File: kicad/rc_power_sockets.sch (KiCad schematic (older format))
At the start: 20 parts, among them IC1 ATTINY85-S, J1 Motion Sensor, J2 Radio 433MHZ, P1 ICSP, Q1 Q_NMOS_GSD, Q2 Q_PMOS_GSD, SW1 Power Switch, U1 MCP1700T-3302E/TT

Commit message: Layout
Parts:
- removed SW1: Power Switch, Buttons_Switches_ThroughHole:SW_Micro_SPST, symbol SWITCH_INV
- added SW1: SPST, Pin_Headers:Pin_Header_Straight_1x02, symbol SPST
- RV1: footprint Potentiometers:Potentiometer_WirePads_largePads -> Potentiometers:Potentiometer_WirePads_Small
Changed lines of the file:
@@
 	4900 5050 4300 5050
 Wire Wire Line
-	4900 5550 4300 5550
+	4300 5550 4900 5550
 Wire Wire Line
 	9100 2450 8750 2450
@@
 	9800 2350 10000 2350
 Wire Wire Line
-	6800 1050 6800 1450
+	6800 1050 6800 1550
 Wire Wire Line
 	4900 5450 4300 5450
@@
 $EndComp
 $Comp
-L SWITCH_INV SW1
-U 1 1 56D9E668
-P 6300 1550
-F 0 "SW1" H 6100 1700 50  0000 C CNN
-F 1 "Power Switch" H 6150 1400 50  0000 C CNN
-F 2 "Buttons_Switches_ThroughHole:SW_Micro_SPST" H 6300 1550 50  0001 C CNN
-F 3 "" H 6300 1550 50  0000 C CNN
-	1    6300 1550
-	1    0    0    -1
-$EndComp
-$Comp
-L GND #PWR08
-U 1 1 56D9E7B6
-P 6800 1650
-F 0 "#PWR08" H 6800 1400 50  0001 C CNN
-F 1 "GND" H 6800 1500 50  0000 C CNN
-F 2 "" H 6800 1650 50  0000 C CNN
-F 3 "" H 6800 1650 50  0000 C CNN
-	1    6800 1650
-	1    0    0    -1
-$EndComp
-$Comp
 L POT RV1
 U 1 1 56E809B9
@@
 F 0 "RV1" H 9650 5220 50  0000 C CNN
 F 1 "POT" H 9650 5300 50  0000 C CNN
-F 2 "Potentiometers:Potentiometer_WirePads_largePads" H 9650 5300 50  0001 C CNN
+F 2 "Potentiometers:Potentiometer_WirePads_Small" H 9650 5300 50  0001 C CNN
 F 3 "" H 9650 5300 50  0000 C CNN
 	1    9650 5300
@@
 $EndComp
 $Comp
-L GND #PWR09
+L GND #PWR08
 U 1 1 56E80AFC
 P 9650 5750
-F 0 "#PWR09" H 9650 5500 50  0001 C CNN
+F 0 "#PWR08" H 9650 5500 50  0001 C CNN
 F 1 "GND" H 9650 5600 50  0000 C CNN
 F 2 "" H 9650 5750 50  0000 C CNN
@@
 $EndComp
 $Comp
-L VCC #PWR010
+L VCC #PWR09
 U 1 1 56E80BFE
 P 6800 1050
-F 0 "#PWR010" H 6800 900 50  0001 C CNN
+F 0 "#PWR09" H 6800 900 50  0001 C CNN
 F 1 "VCC" H 6800 1200 50  0000 C CNN
 F 2 "" H 6800 1050 50  0000 C CNN
@@
 	1    0    0    -1
 $EndComp
+$Comp
+L SPST SW1
+U 1 1 56EAAC50
+P 6300 1550
+F 0 "SW1" H 6300 1650 50  0000 C CNN
+F 1 "SPST" H 6300 1450 50  0000 C CNN
+F 2 "Pin_Headers:Pin_Header_Straight_1x02" H 6300 1550 50  0001 C CNN
+F 3 "" H 6300 1550 50  0000 C CNN
+	1    6300 1550
+	1    0    0    -1
+$EndComp

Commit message: Layout change
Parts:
- removed JP1: Jumper_NO_Small, Pin_Headers:Pin_Header_Straight_1x02, symbol Jumper_NO_Small
- removed R5: 100K, Resistors_SMD:R_0805_HandSoldering, symbol R
- IC1: value ATTINY85-S -> ATTINY85
- J1: value Motion Sensor -> Motion
- J2: value Radio 433MHZ -> 433MHZ
- Q1: value Q_NMOS_GSD -> NMOS
- Q2: value Q_PMOS_GSD -> PMOS
- RV1: symbol POT -> POT-RESCUE-rc_power_sockets
- U1: value MCP1700T-3302E/TT -> MCP1700T
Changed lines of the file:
@@
 EESchema Schematic File Version 2
+LIBS:rc_power_sockets-rescue
 LIBS:power
 LIBS:device
@@
 	1    0    0    -1
 $EndComp
-$Comp
-L Jumper_NO_Small JP1
-U 1 1 56D7129A
-P 9800 2150
-F 0 "JP1" H 9800 2230 50  0000 C CNN
-F 1 "Jumper_NO_Small" H 9810 2090 50  0001 C CNN
-F 2 "Pin_Headers:Pin_Header_Straight_1x02" H 9800 2150 50  0001 C CNN
-F 3 "" H 9800 2150 50  0000 C CNN
-	1    9800 2150
-	0    1    1    0
-$EndComp
 Text Label 4300 5450 0    60   ~ 0
 RADIO_DATA
@@
 P 3000 2050
 F 0 "J1" H 3000 2250 50  0000 C CNN
-F 1 "Motion Sensor" H 3000 1750 50  0000 C CNB
+F 1 "Motion" H 3000 1750 50  0000 C CNB
 F 2 "Socket_Strips:Socket_Strip_Straight_1x03" H 3050 2050 50  0001 C CNN
 F 3 "" H 3050 2050 50  0000 C CNN
@@
 P 9750 3450
 F 0 "J2" H 9750 3250 50  0000 C CNN
-F 1 "Radio 433MHZ" H 9750 3750 50  0000 C CNB
+F 1 "433MHZ" H 9750 3750 50  0000 C CNB
 F 2 "Socket_Strips:Socket_Strip_Straight_1x03" H 9800 3450 50  0001 C CNN
 F 3 "" H 9800 3450 50  0000 C CNN
@@
 	3700 5250 4900 5250
 Wire Wire Line
-	9800 1950 9800 2050
+	9800 1950 9800 2250
 Connection ~ 6550 1950
 Wire Wire Line
@@
 P 6250 5300
 F 0 "IC1" H 5100 5700 50  0000 C CNN
-F 1 "ATTINY85-S" H 7250 4900 50  0000 C CNN
+F 1 "ATTINY85" H 7250 4900 50  0000 C CNN
 F 2 "SMD_Packages:SOIC-8-N" H 7200 5300 50  0000 C CIN
 F 3 "" H 6250 5300 50  0000 C CNN
@@
 $EndComp
 $Comp
-L POT RV1
+L POT-RESCUE-rc_power_sockets RV1
 U 1 1 56E809B9
 P 9650 5300
@@
 L GND #PWR08
 U 1 1 56E80AFC
-P 9650 5750
-F 0 "#PWR08" H 9650 5500 50  0001 C CNN
-F 1 "GND" H 9650 5600 50  0000 C CNN
-F 2 "" H 9650 5750 50  0000 C CNN
-F 3 "" H 9650 5750 50  0000 C CNN
-	1    9650 5750
+P 9650 5450
+F 0 "#PWR08" H 9650 5200 50  0001 C CNN
+F 1 "GND" H 9650 5300 50  0000 C CNN
+F 2 "" H 9650 5450 50  0000 C CNN
+F 3 "" H 9650 5450 50  0000 C CNN
+	1    9650 5450
 	1    0    0    -1
 $EndComp
@@
 Wire Wire Line
 	9650 5050 9650 5150
-$Comp
-L R R5
-U 1 1 56E80FD3
-P 9650 5600
-F 0 "R5" V 9730 5600 50  0000 C CNN
-F 1 "100K" V 9650 5600 50  0000 C CNN
-F 2 "Resistors_SMD:R_0805_HandSoldering" V 9580 5600 50  0001 C CNN
-F 3 "" H 9650 5600 50  0000 C CNN
-	1    9650 5600
-	1    0    0    -1
-$EndComp
 Text Label 4300 5350 0    60   ~ 0
 ADC3
@@
 P 6450 2450
 F 0 "Q2" H 6750 2500 50  0000 R CNN
-F 1 "Q_PMOS_GSD" H 7100 2400 50  0000 R CNN
+F 1 "PMOS" H 6850 2400 50  0000 R CNN
 F 2 "TO_SOT_Packages_SMD:SOT-23_Handsoldering" H 6650 2550 50  0001 C CNN
 F 3 "" H 6450 2450 50  0000 C CNN
@@
 P 5450 3150
 F 0 "Q1" H 5750 3200 50  0000 R CNN
-F 1 "Q_NMOS_GSD" H 6100 3100 50  0000 R CNN
+F 1 "NMOS" H 5850 3100 50  0000 R CNN
 F 2 "TO_SOT_Packages_SMD:SOT-23_Handsoldering" H 5650 3250 50  0001 C CNN
 F 3 "" H 5450 3150 50  0000 C CNN
@@
 P 7350 3900
 F 0 "U1" H 7500 3600 50  0000 C CNN
-F 1 "MCP1700T-3302E/TT" H 7350 4100 50  0000 C CNN
+F 1 "MCP1700T" H 7350 4100 50  0000 C CNN
 F 2 "TO_SOT_Packages_SMD:SOT-23_Handsoldering" H 7350 4000 50  0000 C CIN
 F 3 "" H 7350 3900 50  0000 C CNN

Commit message: Traces
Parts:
- removed P1: ICSP, Pin_Headers:Pin_Header_Straight_2x03, symbol DIL6
- added J3: 433MHZ, Socket_Strips:Socket_Strip_Straight_1x03, symbol SIL3
- added P1: ICSP, Pin_Headers:Pin_Header_Straight_2x03, symbol CONN_02X03
- added P2: CONN_GND, Pin_Headers:Pin_Header_Straight_1x01, symbol CONN_01X01
- J1: value Motion -> PIR
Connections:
- net GND: now also J3.1, P1.6 (P6), P2.1 (P1)
- net MISO: now also P1.1 (P1)
- net MOSI: now also P1.4 (P4)
- net RADIO_DATA: now also J2.3, J3.3; no longer J2.2
- net RESET: now also RV1.3, P1.5 (P5)
- net SCK: now also P1.3 (P3)
- net NBASE: now reaches Q1.1 (G), R1.1, R3.1
- net NBASE_ON: now reaches D1.1 (K), D2.1 (K), R1.2
- net POWER: now reaches J1.3, Q2.3 (D), R2.1, SW1.1
- net POWER: now also P1.2 (P2)
- net PBASE: now reaches Q1.3 (D), Q2.1 (G), R2.2
- net 3.3v: now reaches C2.1, C3.1, IC1.8 (VCC), R4.2, U1.2 (VOUT)
- net 3.3v: no longer RV1.3
- net SWITCH_POWER: now reaches C1.1, Q2.2 (S), U1.3 (VIN)
- net SWITCH_POWER: now also J2.2, J3.2; no longer J2.3
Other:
- moved on the sheet: RV1
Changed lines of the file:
@@
 Text Label 4300 5550 0    60   ~ 0
 RESET
-Text Label 10000 2350 0    60   ~ 0
+Text Label 8600 2300 0    60   ~ 0
 MOSI
-Text Label 8750 2250 0    60   ~ 0
+Text Label 7650 2200 0    60   ~ 0
 MISO
-Text Label 8750 2450 0    60   ~ 0
+Text Label 7650 2400 0    60   ~ 0
 RESET
-$Comp
-L DIL6 P1
-U 1 1 56D70BCB
-P 9450 2350
-F 0 "P1" H 9450 2550 50  0000 C CNN
-F 1 "ICSP" H 9450 2100 50  0000 C CNB
-F 2 "Pin_Headers:Pin_Header_Straight_2x03" H 9450 2350 50  0001 C CNN
-F 3 "" H 9450 2350 50  0000 C CNN
-	1    9450 2350
-	1    0    0    -1
-$EndComp
-Text Label 8750 2350 0    60   ~ 0
+Text Label 7650 2300 0    60   ~ 0
 SCK
 $Comp
 L GND #PWR04
 U 1 1 56D7102B
-P 9800 2450
-F 0 "#PWR04" H 9800 2200 50  0001 C CNN
-F 1 "GND" H 9800 2300 50  0000 C CNN
-F 2 "" H 9800 2450 50  0000 C CNN
-F 3 "" H 9800 2450 50  0000 C CNN
-	1    9800 2450
+P 8450 2400
+F 0 "#PWR04" H 8450 2150 50  0001 C CNN
+F 1 "GND" H 8450 2250 50  0000 C CNN
+F 2 "" H 8450 2400 50  0000 C CNN
+F 3 "" H 8450 2400 50  0000 C CNN
+	1    8450 2400
 	1    0    0    -1
 $EndComp
@@
 P 3000 2050
 F 0 "J1" H 3000 2250 50  0000 C CNN
-F 1 "Motion" H 3000 1750 50  0000 C CNB
+F 1 "PIR" H 3000 1750 50  0000 C CNB
 F 2 "Socket_Strips:Socket_Strip_Straight_1x03" H 3050 2050 50  0001 C CNN
 F 3 "" H 3050 2050 50  0000 C CNN
@@
 	1    0    0    1
 $EndComp
-Text Label 8850 3450 0    60   ~ 0
+Text Label 8850 3350 0    60   ~ 0
 RADIO_DATA
 $Comp
@@
 	1    0    0    -1
 $EndComp
-Connection ~ 5550 1950
-Wire Wire Line
-	5550 2450 6250 2450
-Wire Wire Line
-	5550 2400 5550 2950
-Wire Wire Line
-	6550 1950 6550 2250
-Connection ~ 5550 2450
-Wire Wire Line
-	6550 3850 6900 3850
-Connection ~ 6700 3850
-Wire Wire Line
-	7800 3850 8600 3850
-Wire Wire Line
-	7350 4200 7350 4400
-Wire Wire Line
-	6700 4150 6700 4300
-Wire Wire Line
-	6700 4300 8000 4300
-Connection ~ 7350 4300
-Wire Wire Line
-	8000 4300 8000 4150
-Wire Wire Line
-	8600 3850 8600 5950
-Wire Wire Line
-	7600 5050 9650 5050
-Connection ~ 8000 3850
-Wire Wire Line
-	4150 3050 4150 3300
-Connection ~ 4150 3150
-Wire Wire Line
-	4150 2050 4150 2750
-Wire Wire Line
-	4150 5150 4900 5150
-Wire Wire Line
-	4900 5050 4300 5050
-Wire Wire Line
-	4300 5550 4900 5550
-Wire Wire Line
-	9100 2450 8750 2450
-Wire Wire Line
-	9100 2350 8750 2350
-Wire Wire Line
-	9100 2250 8750 2250
-Wire Wire Line
-	9800 2350 10000 2350
-Wire Wire Line
-	6800 1050 6800 1550
-Wire Wire Line
-	4900 5450 4300 5450
-Wire Wire Line
-	3350 1950 9800 1950
-Wire Wire Line
-	4150 3600 4150 5150
-Wire Wire Line
-	5550 1550 5800 1550
-Wire Wire Line
-	4650 3150 4150 3150
-Wire Wire Line
-	4950 3150 5250 3150
-Wire Wire Line
-	6550 2650 6550 3850
-Wire Wire Line
-	9400 3450 8850 3450
-Wire Wire Line
-	3350 2050 4150 2050
-Wire Wire Line
-	3700 2050 3700 5250
-Connection ~ 3700 2050
-Wire Wire Line
-	3700 5250 4900 5250
-Wire Wire Line
-	9800 1950 9800 2250
-Connection ~ 6550 1950
-Wire Wire Line
-	5550 1550 5550 2100
-Connection ~ 6550 3350
-Wire Wire Line
-	5550 3350 5550 3800
 $Comp
 L R R3
@@
 	1    0    0    -1
 $EndComp
-Wire Wire Line
-	5150 3650 5550 3650
-Connection ~ 5550 3650
-Wire Wire Line
-	5150 3350 5150 3150
-Connection ~ 5150 3150
 $Comp
 L R R4
@@
 	1    0    0    -1
 $EndComp
-Wire Wire Line
-	4750 5650 4750 5550
-Connection ~ 4750 5550
-Wire Wire Line
-	8600 5950 4750 5950
-Connection ~ 8600 5050
-Wire Wire Line
-	9400 3350 6550 3350
 $Comp
 L C C3
@@
 	1    0    0    -1
 $EndComp
-Wire Wire Line
-	8250 5200 8250 5050
-Connection ~ 8250 5050
 $Comp
 L GND #PWR07
@@
 L POT-RESCUE-rc_power_sockets RV1
 U 1 1 56E809B9
-P 9650 5300
-F 0 "RV1" H 9650 5220 50  0000 C CNN
-F 1 "POT" H 9650 5300 50  0000 C CNN
-F 2 "Potentiometers:Potentiometer_WirePads_Small" H 9650 5300 50  0001 C CNN
-F 3 "" H 9650 5300 50  0000 C CNN
-	1    9650 5300
+P 4100 6050
+F 0 "RV1" H 4100 5970 50  0000 C CNN
+F 1 "POT" H 4100 6050 50  0000 C CNN
+F 2 "Potentiometers:Potentiometer_WirePads_Small" H 4100 6050 50  0001 C CNN
+F 3 "" H 4100 6050 50  0000 C CNN
+	1    4100 6050
 	0    -1   -1   0
 $EndComp
@@
 L GND #PWR08
 U 1 1 56E80AFC
-P 9650 5450
-F 0 "#PWR08" H 9650 5200 50  0001 C CNN
-F 1 "GND" H 9650 5300 50  0000 C CNN
-F 2 "" H 9650 5450 50  0000 C CNN
-F 3 "" H 9650 5450 50  0000 C CNN
-	1    9650 5450
+P 4100 6200
+F 0 "#PWR08" H 4100 5950 50  0001 C CNN
+F 1 "GND" H 4100 6050 50  0000 C CNN
+F 2 "" H 4100 6200 50  0000 C CNN
+F 3 "" H 4100 6200 50  0000 C CNN
+	1    4100 6200
 	1    0    0    -1
 $EndComp
@@
 	1    0    0    -1
 $EndComp
-Wire Wire Line
-	9650 5050 9650 5150
 Text Label 4300 5350 0    60   ~ 0
 ADC3
-Text Label 9200 5300 0    60   ~ 0
+Text Label 3650 6050 0    60   ~ 0
 ADC3
-Wire Wire Line
-	9500 5300 9200 5300
-Wire Wire Line
-	4900 5350 4300 5350
 $Comp
 L Q_PMOS_GSD Q2
@@
 	1    0    0    -1
 $EndComp
+$Comp
+L CONN_02X03 P1
+U 1 1 56EEE1EA
+P 8200 2300
+F 0 "P1" H 8200 2500 50  0000 C CNN
+F 1 "ICSP" H 8200 2100 50  0000 C CNN
+F 2 "Pin_Headers:Pin_Header_Straight_2x03" H 8200 1100 50  0001 C CNN
+F 3 "" H 8200 1100 50  0000 C CNN
+	1    8200 2300
+	1    0    0    -1
+$EndComp
+Text Label 4200 3150 0    60   ~ 0
+NBASE_ON
+Text Label 5850 2450 0    60   ~ 0
+PBASE
+Text Label 8600 4400 0    60   ~ 0
+3.3v
+Text Label 6550 3050 0    60   ~ 0
+SWITCH_POWER
+Text Label 4600 1950 0    60   ~ 0
+POWER
+Text Label 5000 3150 0    60   ~ 0
+NBASE
+$Comp
+L CONN_01X01 P2
+U 1 1 56EEF3F5
+P 7200 1000
+F 0 "P2" V 7150 900 50  0000 C CNN
+F 1 "CONN_GND" V 7300 1000 50  0000 C CNN
+F 2 "Pin_Headers:Pin_Header_Straight_1x01" H 7200 1000 50  0001 C CNN
+F 3 "" H 7200 1000 50  0000 C CNN
+	1    7200 1000
+	0    -1   -1   0
+$EndComp
+$Comp
+L GND #PWR010
+U 1 1 56EEF4F7
+P 7200 1200
+F 0 "#PWR010" H 7200 950 50  0001 C CNN
+F 1 "GND" H 7200 1050 50  0000 C CNN
+F 2 "" H 7200 1200 50  0000 C CNN
+F 3 "" H 7200 1200 50  0000 C CNN
+	1    7200 1200
+	1    0    0    -1
+$EndComp
+$Comp
+L SIL3 J3
+U 1 1 56EEFA66
+P 9750 2800
+F 0 "J3" H 9750 2600 50  0000 C CNN
+F 1 "433MHZ" H 9750 3100 50  0000 C CNB
+F 2 "Socket_Strips:Socket_Strip_Straight_1x03" H 9800 2800 50  0001 C CNN
+F 3 "" H 9800 2800 50  0000 C CNN
+	1    9750 2800
+	1    0    0    1
+$EndComp
+Text Label 8850 2700 0    60   ~ 0
+RADIO_DATA
+$Comp
+L GND #PWR011
+U 1 1 56EEFB0C
+P 9400 2900
+F 0 "#PWR011" H 9400 2650 50  0001 C CNN
+F 1 "GND" H 9400 2750 50  0000 C CNN
+F 2 "" H 9400 2900 50  0000 C CNN
+F 3 "" H 9400 2900 50  0000 C CNN
+	1    9400 2900
+	1    0    0    -1
+$EndComp
+Connection ~ 5550 1950
+Wire Wire Line
+	5550 2450 6250 2450
+Wire Wire Line
+	5550 2400 5550 2950
+Wire Wire Line
+	6550 1950 6550 2250
+Connection ~ 5550 2450
+Wire Wire Line
+	6550 3850 6900 3850
+Connection ~ 6700 3850
+Wire Wire Line
+	7800 3850 8600 3850
+Wire Wire Line
+	7350 4200 7350 4400
+Wire Wire Line
+	6700 4150 6700 4300
+Wire Wire Line
+	6700 4300 8000 4300
+Connection ~ 7350 4300
+Wire Wire Line
+	8000 4300 8000 4150
+Wire Wire Line
+	8600 3850 8600 5950
+Connection ~ 8000 3850
+Wire Wire Line
+	4150 3050 4150 3300
+Connection ~ 4150 3150
+Wire Wire Line
+	4150 2050 4150 2750
+Wire Wire Line
+	4150 5150 4900 5150
+Wire Wire Line
+	4900 5050 4300 5050
+Wire Wire Line
+	4100 5550 4900 5550
+Wire Wire Line
+	6800 1050 6800 1550
+Wire Wire Line
+	4900 5450 4300 5450
+Wire Wire Line
+	3350 1950 8650 1950
+Wire Wire Line
+	4150 3600 4150 5150
+Wire Wire Line
+	5550 1550 5800 1550
+Wire Wire Line
+	4650 3150 4150 3150
+Wire Wire Line
+	4950 3150 5250 3150
+Wire Wire Line
+	6550 2650 6550 3850
+Wire Wire Line
+	6550 3450 9400 3450
+Wire Wire Line
+	3350 2050 4150 2050
+Wire Wire Line
+	3700 5250 4900 5250
+Connection ~ 6550 1950
+Wire Wire Line
+	5550 1550 5550 2100
+Wire Wire Line
+	5550 3350 5550 3800
+Wire Wire Line
+	5150 3650 5550 3650
+Connection ~ 5550 3650
+Wire Wire Line
+	5150 3350 5150 3150
+Connection ~ 5150 3150
+Wire Wire Line
+	4750 5650 4750 5550
+Connection ~ 4750 5550
+Wire Wire Line
+	8600 5950 4750 5950
+Connection ~ 8600 5050
+Wire Wire Line
+	8250 5200 8250 5050
+Connection ~ 8250 5050
+Wire Wire Line
+	3950 6050 3650 6050
+Wire Wire Line
+	4900 5350 4300 5350
+Connection ~ 6550 3450
+Wire Wire Line
+	8850 3350 9400 3350
+Wire Wire Line
+	8450 2300 8600 2300
+Wire Wire Line
+	8450 2200 8650 2200
+Wire Wire Line
+	8650 2200 8650 1950
+Wire Wire Line
+	7950 2200 7650 2200
+Wire Wire Line
+	7650 2300 7950 2300
+Wire Wire Line
+	7650 2400 7950 2400
+Wire Wire Line
+	3700 2050 3700 5250
+Connection ~ 3700 2050
+Wire Wire Line
+	9400 2700 8850 2700
+Wire Wire Line
+	9400 2800 8500 2800
+Wire Wire Line
+	8500 2800 8500 3450
+Connection ~ 8500 3450
+Wire Wire Line
+	7600 5050 8600 5050
+Wire Wire Line
+	4100 5550 4100 5900
 $EndSCHEMATC

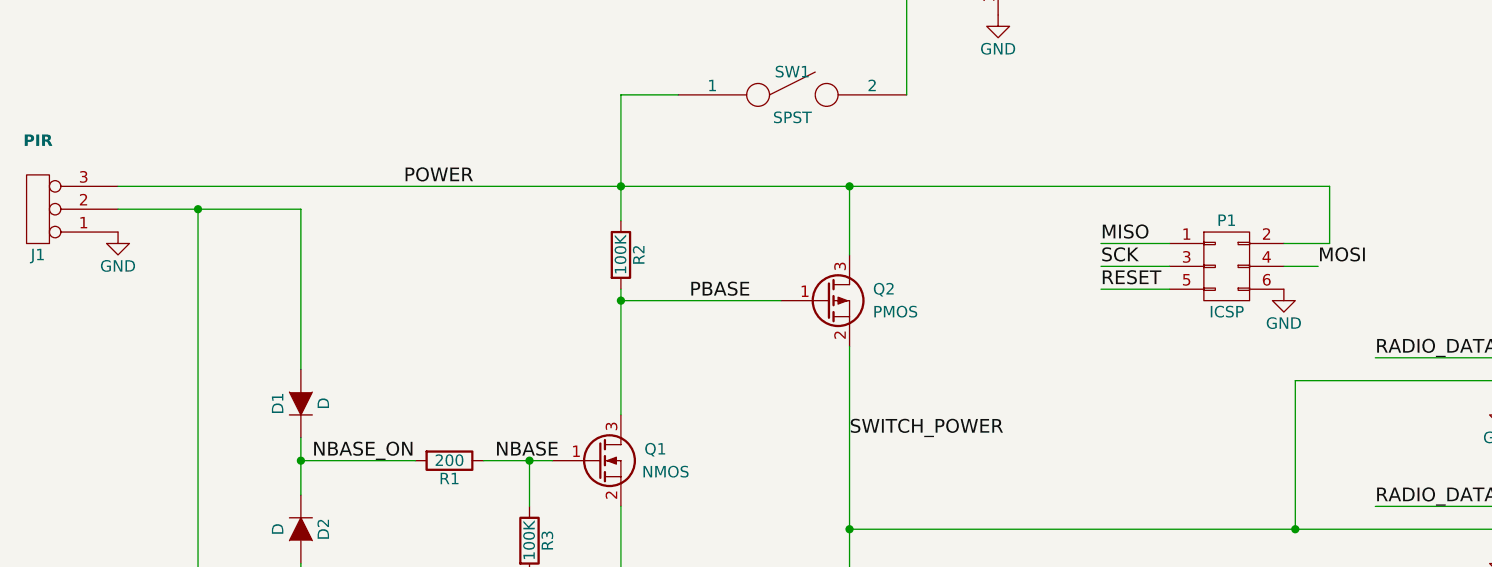
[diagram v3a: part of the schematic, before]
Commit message: Switched power plane
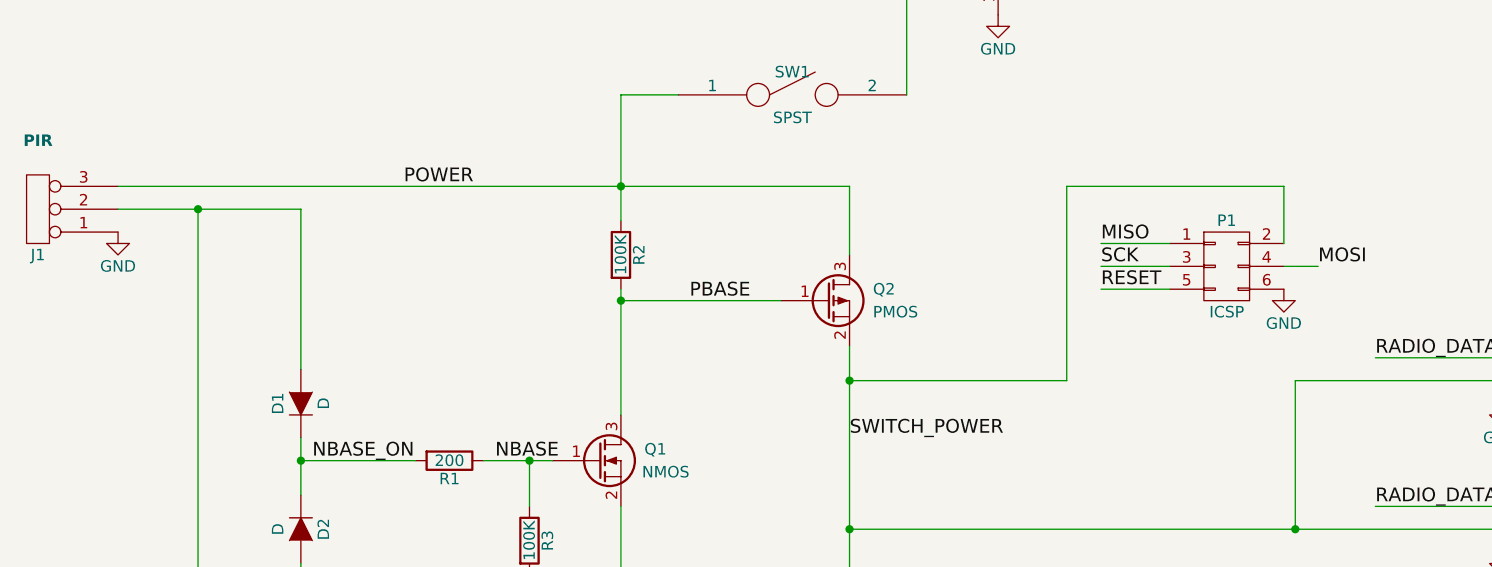
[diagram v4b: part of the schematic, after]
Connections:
- net POWER: no longer P1.2 (P2)
- net SWITCH_POWER: now also P1.2 (P2)
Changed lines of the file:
@@
 	4900 5450 4300 5450
 Wire Wire Line
-	3350 1950 8650 1950
+	3350 1950 6550 1950
 Wire Wire Line
 	4150 3600 4150 5150
@@
 Wire Wire Line
 	3700 5250 4900 5250
-Connection ~ 6550 1950
 Wire Wire Line
 	5550 1550 5550 2100
@@
 	8450 2300 8600 2300
 Wire Wire Line
-	8450 2200 8650 2200
-Wire Wire Line
-	8650 2200 8650 1950
-Wire Wire Line
 	7950 2200 7650 2200
 Wire Wire Line
@@
 Wire Wire Line
 	4100 5550 4100 5900
+Wire Wire Line
+	8450 2200 8450 1950
+Wire Wire Line
+	8450 1950 7500 1950
+Wire Wire Line
+	7500 1950 7500 2800
+Wire Wire Line
+	7500 2800 6550 2800
+Connection ~ 6550 2800
 $EndSCHEMATC

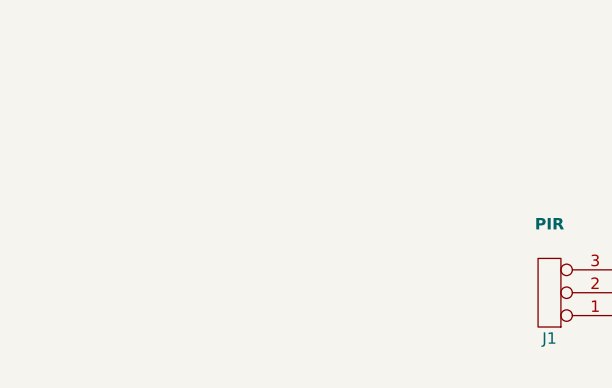
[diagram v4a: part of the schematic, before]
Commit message: Grounded mounting holes
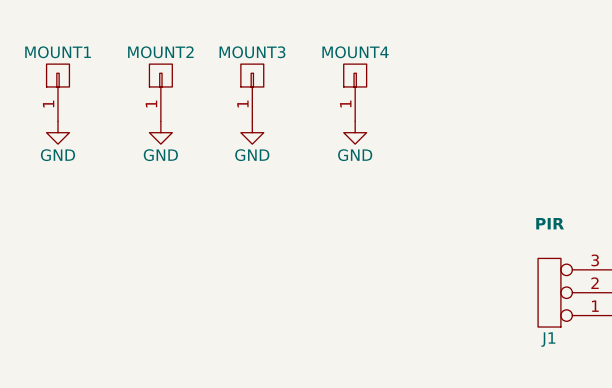
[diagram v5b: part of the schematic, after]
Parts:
- added MOUNT1, MOUNT2, MOUNT3, MOUNT4: CONN_01X01, symbol CONN_01X01
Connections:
- net GND: now also MOUNT1.1 (P1), MOUNT2.1 (P1), MOUNT3.1 (P1), MOUNT4.1 (P1)
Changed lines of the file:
@@
 	7500 2800 6550 2800
 Connection ~ 6550 2800
+$Comp
+L CONN_01X01 MOUNT3
+U 1 1 56F02C78
+P 1700 1100
+F 0 "MOUNT3" V 1800 1100 50  0000 C CNN
+F 1 "CONN_01X01" V 1600 800 50  0001 C CNN
+F 2 "" H 1700 1100 50  0000 C CNN
+F 3 "" H 1700 1100 50  0000 C CNN
+	1    1700 1100
+	0    -1   -1   0
+$EndComp
+$Comp
+L GND #PWR012
+U 1 1 56F02CD0
+P 1700 1300
+F 0 "#PWR012" H 1700 1050 50  0001 C CNN
+F 1 "GND" H 1700 1150 50  0000 C CNN
+F 2 "" H 1700 1300 50  0000 C CNN
+F 3 "" H 1700 1300 50  0000 C CNN
+	1    1700 1300
+	1    0    0    -1
+$EndComp
+$Comp
+L CONN_01X01 MOUNT4
+U 1 1 56F02EEA
+P 2150 1100
+F 0 "MOUNT4" V 2250 1100 50  0000 C CNN
+F 1 "CONN_01X01" V 2050 800 50  0001 C CNN
+F 2 "" H 2150 1100 50  0000 C CNN
+F 3 "" H 2150 1100 50  0000 C CNN
+	1    2150 1100
+	0    -1   -1   0
+$EndComp
+$Comp
+L GND #PWR013
+U 1 1 56F02EF0
+P 2150 1300
+F 0 "#PWR013" H 2150 1050 50  0001 C CNN
+F 1 "GND" H 2150 1150 50  0000 C CNN
+F 2 "" H 2150 1300 50  0000 C CNN
+F 3 "" H 2150 1300 50  0000 C CNN
+	1    2150 1300
+	1    0    0    -1
+$EndComp
+$Comp
+L CONN_01X01 MOUNT1
+U 1 1 56F02F70
+P 850 1100
+F 0 "MOUNT1" V 950 1100 50  0000 C CNN
+F 1 "CONN_01X01" V 750 800 50  0001 C CNN
+F 2 "" H 850 1100 50  0000 C CNN
+F 3 "" H 850 1100 50  0000 C CNN
+	1    850  1100
+	0    -1   -1   0
+$EndComp
+$Comp
+L GND #PWR014
+U 1 1 56F02F76
+P 850 1300
+F 0 "#PWR014" H 850 1050 50  0001 C CNN
+F 1 "GND" H 850 1150 50  0000 C CNN
+F 2 "" H 850 1300 50  0000 C CNN
+F 3 "" H 850 1300 50  0000 C CNN
+	1    850  1300
+	1    0    0    -1
+$EndComp
+$Comp
+L CONN_01X01 MOUNT2
+U 1 1 56F02F7C
+P 1300 1100
+F 0 "MOUNT2" V 1400 1100 50  0000 C CNN
+F 1 "CONN_01X01" V 1200 800 50  0001 C CNN
+F 2 "" H 1300 1100 50  0000 C CNN
+F 3 "" H 1300 1100 50  0000 C CNN
+	1    1300 1100
+	0    -1   -1   0
+$EndComp
+$Comp
+L GND #PWR015
+U 1 1 56F02F82
+P 1300 1300
+F 0 "#PWR015" H 1300 1050 50  0001 C CNN
+F 1 "GND" H 1300 1150 50  0000 C CNN
+F 2 "" H 1300 1300 50  0000 C CNN
+F 3 "" H 1300 1300 50  0000 C CNN
+	1    1300 1300
+	1    0    0    -1
+$EndComp
 $EndSCHEMATC
